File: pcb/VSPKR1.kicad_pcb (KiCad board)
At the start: 2 copper layers, 210 x 80 mm, 30 parts, among them J1 USB_C_Receptacle_USB2.0_14P, J2 Screw_Terminal_01x02, J3 Screw_Terminal_01x02, SW1 RESET, SW2 BOOT, U1 ESP32-S3-WROOM-1, U2 AMS1117-3.3, U3 PCM5102A, U4 PAM8403D

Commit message: pcb
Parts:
- added H1: MountingHole, MountingHole:MountingHole_2.2mm_M2, F.Cu at (80.0, 45.0)
- added H2: MountingHole, MountingHole:MountingHole_2.2mm_M2, F.Cu at (210.0, 45.0)
- added H3: MountingHole, MountingHole:MountingHole_2.2mm_M2, F.Cu at (80.0, 115.0)
- added H4: MountingHole, MountingHole:MountingHole_2.2mm_M2, F.Cu at (210.0, 115.0)
- moved SW2 142.5 mm to (166.5, 111.5)
- moved J2 137.7 mm to (174.5, 99.2)
- moved C1 111.1 mm to (104.0, 52.0)
- moved C3 111.1 mm to (104.0, 58.0)
- moved C4 111.1 mm to (104.0, 61.0)
- moved R3 111.1 mm to (99.2, 57.9)
- moved R5 111.1 mm to (99.2, 63.8)
- moved R8 111.1 mm to (99.2, 72.6)
- moved C11 111.1 mm to (113.6, 58.0)
- moved C12 111.1 mm to (113.6, 61.0)
- moved C5 111.1 mm to (108.8, 52.0)
- moved C7 111.1 mm to (108.8, 58.0)
- moved C8 111.1 mm to (108.8, 61.0)
- moved C9 111.1 mm to (113.6, 52.0)
- moved MK1 111.1 mm to (90.2, 68.2)
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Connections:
- C5 pad 2: unconnected-(C5-Pad2) -> GND
- C7 pad 2: +3V3 -> GND
- C8 pad 2: Net-(C8-Pad2) -> GND
- C9 pad 1: Net-(C8-Pad2) -> Net-(U3-LDOO)
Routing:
- net GND: track 27.0 -> 1.56 mm
- net +3V3: track 15.5 -> 0.00 mm, vias 4 -> 0
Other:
- board size 210 x 80 mm -> 140 x 80 mm

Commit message: git push -m "hmm"
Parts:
- added C13: 0.1uF, Capacitor_SMD:C_0805_2012Metric_Pad1.18x1.45mm_HandSolder, F.Cu at (90.0, 66.5)
- moved R2 74.6 mm to (151.0, 108.5), turned to 180 degrees
- moved R1 69.2 mm to (139.0, 108.5)
- moved MK1 59.6 mm to (30.7, 64.7)
- moved U3 57.4 mm to (173.5, 77.9)
- moved U2 46.9 mm to (145.0, 103.5), turned to 90 degrees
- moved U4 33.6 mm to (116.5, 75.8)
- moved C1 14.1 mm to (90.0, 54.5)
- moved C2 14.1 mm to (90.0, 57.5)
- moved C3 14.1 mm to (90.0, 60.5)
- moved C4 14.1 mm to (90.0, 63.5)
- moved R3 14.1 mm to (85.3, 60.4)
- moved R4 14.1 mm to (85.3, 63.3)
- moved R5 14.1 mm to (85.3, 66.2)
- moved R6 14.1 mm to (85.3, 69.2)
- moved R7 14.1 mm to (85.3, 72.2)
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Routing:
- net GND: track 1.56 -> 113.9 mm, vias 0 -> 2
- net Net-(J3-Pin_1): track 0.00 -> 39.8 mm, vias 0 -> 2
- net Net-(J3-Pin_2): track 0.00 -> 35.9 mm
- net +5V: track 0.00 -> 25.0 mm, vias 0 -> 2
- net +3V3: track 0.00 -> 23.4 mm, vias 0 -> 2
- net /CHIP_PU: track 0.00 -> 14.3 mm
- net /IO0: track 0.00 -> 14.3 mm
- net Net-(J1-CC1): track 0.00 -> 9.23 mm, vias 0 -> 2
- net Net-(J1-CC2): track 0.00 -> 8.73 mm, vias 0 -> 2
- net (no net): track 0.00 -> 6.87 mm
- net /D+: track 0.00 -> 6.45 mm, vias 0 -> 2
- net /D-: track 0.00 -> 3.67 mm

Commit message: Routing PCB traces
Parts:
- moved C9 87.7 mm to (184.5, 76.5), turned to -90 degrees
- moved C8 87.1 mm to (181.0, 76.5), turned to -90 degrees
- moved C7 74.0 mm to (167.0, 77.0), turned to 90 degrees
- moved C6 70.9 mm to (163.0, 77.0), turned to -90 degrees
- moved R8 23.4 mm to (108.0, 80.5), turned to -90 degrees
- moved R7 21.0 mm to (104.5, 80.5), turned to -90 degrees
- moved U2 1.00 mm to (145.0, 102.5)
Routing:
- net GND: track 113.9 -> 332.6 mm, vias 2 -> 11
- net /CHIP_PU: track 14.3 -> 169.0 mm, vias 0 -> 2
- net +3V3: track 23.4 -> 177.5 mm, vias 2 -> 10
- net Net-(J2-Pin_2): track 0.00 -> 124.9 mm, vias 0 -> 3
- net Net-(J2-Pin_1): track 0.00 -> 118.7 mm
- net /LEFT-CHANNEL-OUT: track 0.00 -> 114.5 mm, vias 0 -> 2
- net /WS: track 0.00 -> 103.7 mm, vias 0 -> 2
- net /RIGHT-CHANNEL-OUT: track 0.00 -> 97.3 mm, vias 0 -> 2
- net Net-(U1-IO5): track 0.00 -> 95.6 mm, vias 0 -> 2
- net /DOUT: track 0.00 -> 91.6 mm, vias 0 -> 4
- net /BCK: track 0.04 -> 74.0 mm, vias 0 -> 2
- net +5V: track 25.0 -> 97.6 mm, vias 2 -> 4
- net /D+: track 6.45 -> 58.0 mm, vias 2 -> 4
- net /D-: track 3.67 -> 47.0 mm, vias 0 -> 2
- net /IO0: track 14.3 -> 57.6 mm, vias 0 -> 2
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
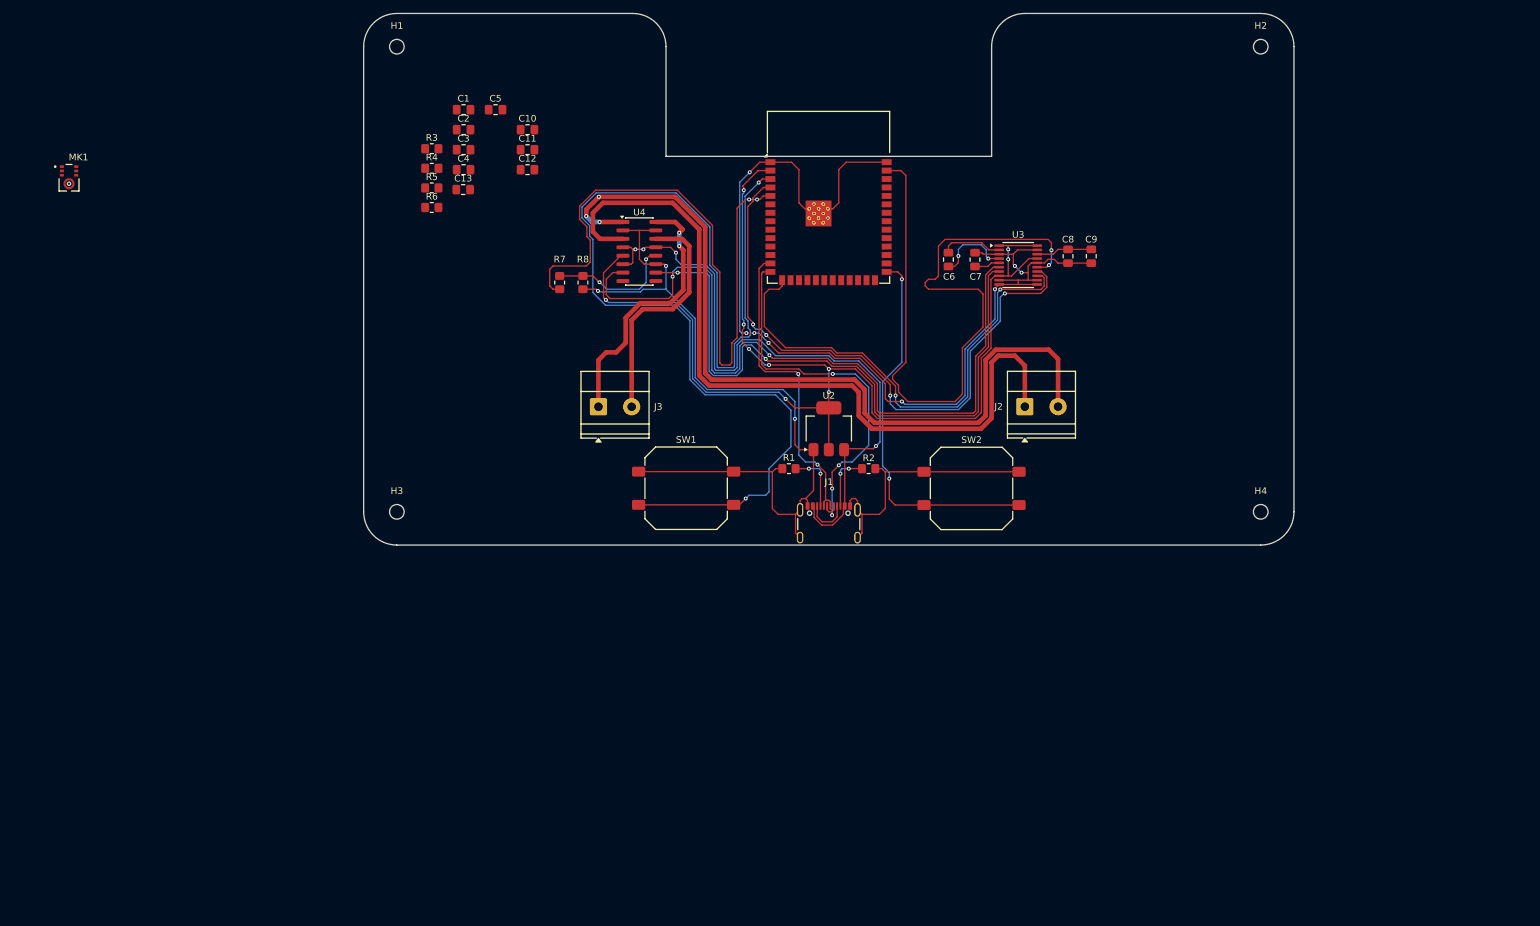
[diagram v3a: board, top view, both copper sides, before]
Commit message: Finished  the PCB
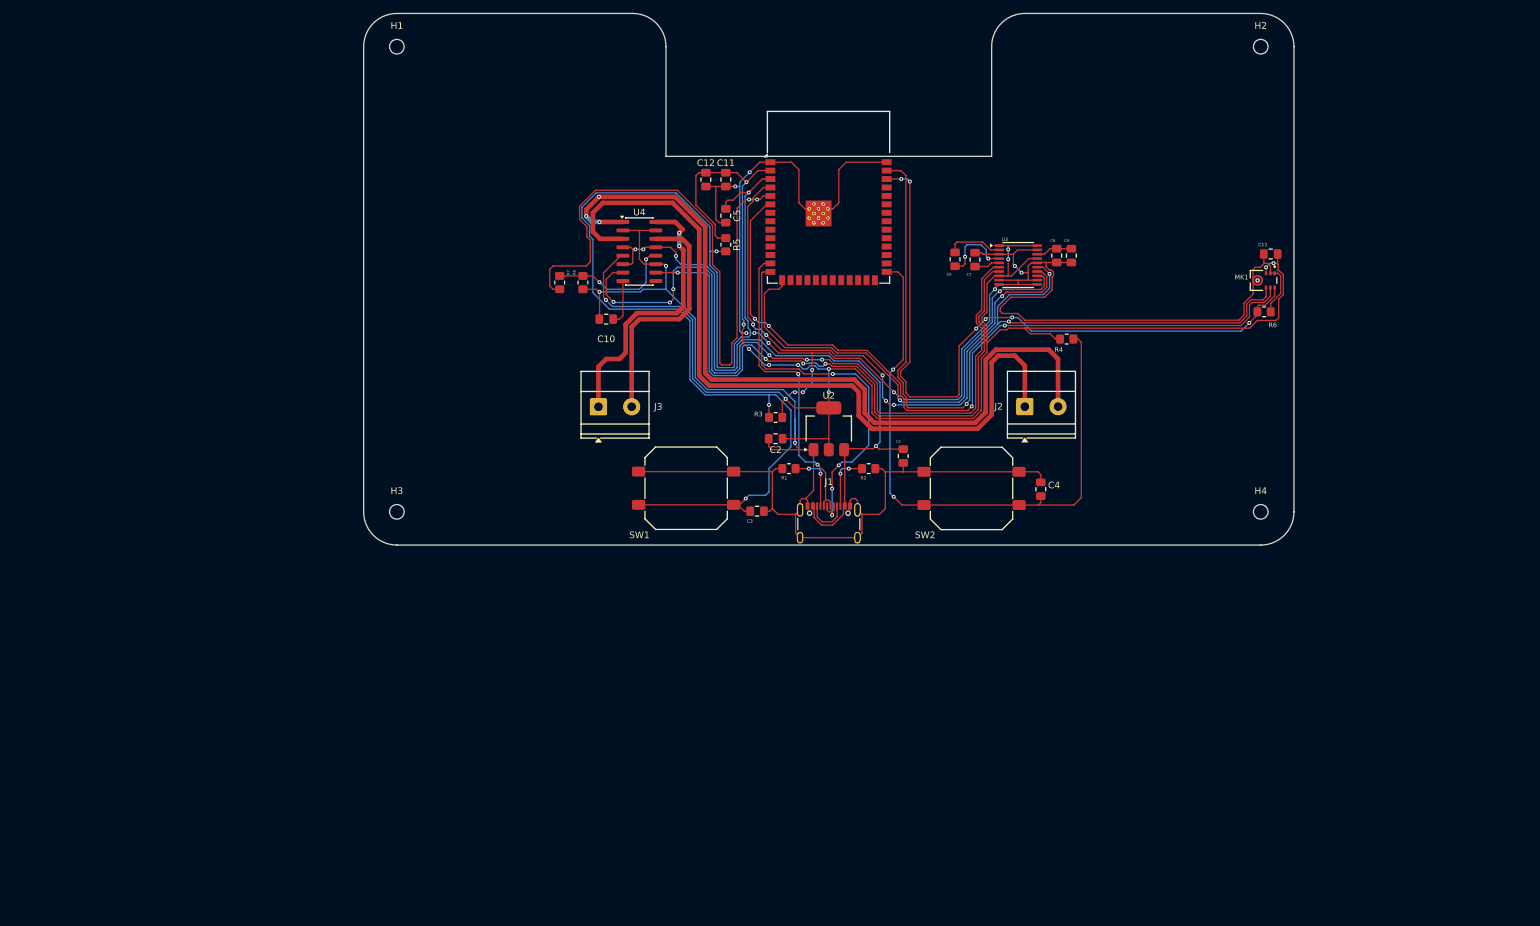
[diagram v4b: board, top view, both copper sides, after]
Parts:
- moved MK1 180.4 mm to (210.4, 80.2), turned to -90 degrees
- moved R6 126.2 mm to (210.5, 84.9)
- moved C13 121.9 mm to (211.5, 76.2), turned to 180 degrees
- moved C4 99.3 mm to (176.9, 111.6), turned to -90 degrees
- moved R4 98.9 mm to (180.8, 89.0)
- moved C1 84.2 mm to (156.2, 106.6), turned to -90 degrees
- moved C3 70.1 mm to (134.2, 114.9), turned to 180 degrees
- moved C2 66.1 mm to (137.0, 104.0), turned to 180 degrees
- moved R3 65.7 mm to (137.0, 100.8), turned to 180 degrees
- moved R5 45.1 mm to (129.5, 74.8), turned to -90 degrees
- moved C5 38.2 mm to (129.5, 70.4), turned to -90 degrees
- moved C10 30.9 mm to (111.5, 86.0), turned to 180 degrees
- moved C11 30.2 mm to (129.5, 65.0), turned to -90 degrees
- moved C12 26.9 mm to (126.5, 65.0), turned to -90 degrees
- moved C9 3.00 mm to (181.5, 76.4)
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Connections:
- U1 pad 6: unconnected-(U1-IO6-Pad6) -> /SCK
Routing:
- net /SCK: track 0.00 -> 118.2 mm, vias 0 -> 4
- net GND: track 332.6 -> 449.7 mm, vias 11 -> 15
- net /SD: track 0.00 -> 106.4 mm, vias 0 -> 6
- net +3V3: track 177.5 -> 273.6 mm, vias 10 -> 13
- net /IO0: track 57.6 -> 92.4 mm
- net /WS: track 103.7 -> 123.2 mm, vias 2 -> 3
- net /CHIP_PU: track 169.0 -> 182.7 mm, vias 2 -> 4
- net Net-(U4-VREF): track 0.00 -> 6.91 mm
- net +5V: track 97.6 -> 101.9 mm
- net Net-(U3-LDOO): track 8.44 -> 5.28 mm
- net /LEFT-CHANNEL-OUT: track 114.5 -> 115.9 mm, vias 2 -> 6
- net Net-(J3-Pin_1): track 40.4 -> 41.6 mm
- net /BCK: track 74.0 -> 73.0 mm
- net /RIGHT-CHANNEL-OUT: track 97.3 -> 98.2 mm, vias 2 -> 4
- net Net-(J3-Pin_2): track 35.9 -> 36.8 mm
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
